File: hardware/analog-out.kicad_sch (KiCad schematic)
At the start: 14 parts, among them U9 TL072

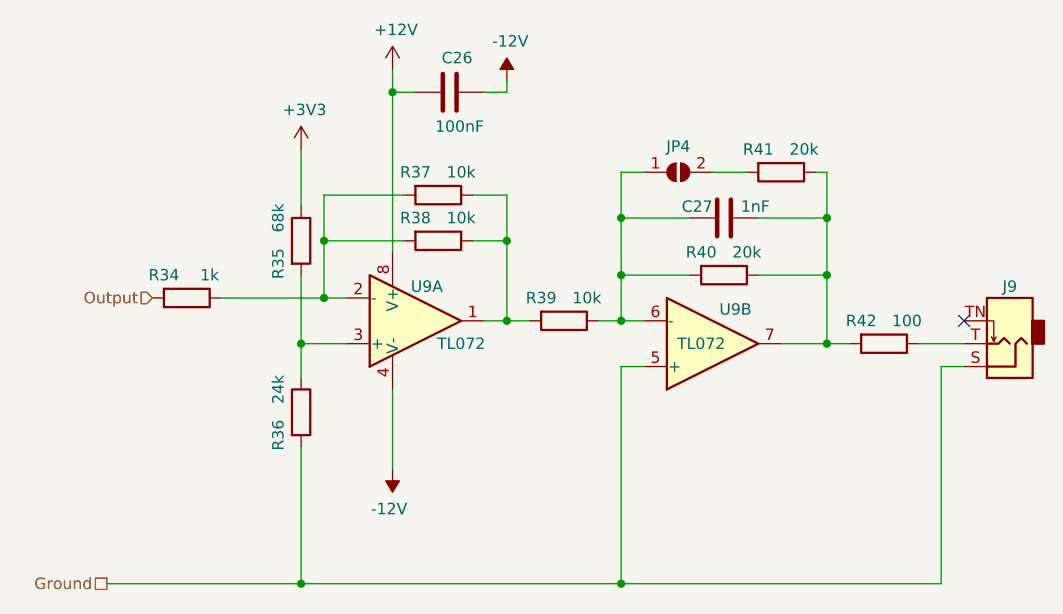
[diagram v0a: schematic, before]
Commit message: First cut of the software. Not changed to RISC-V yet.
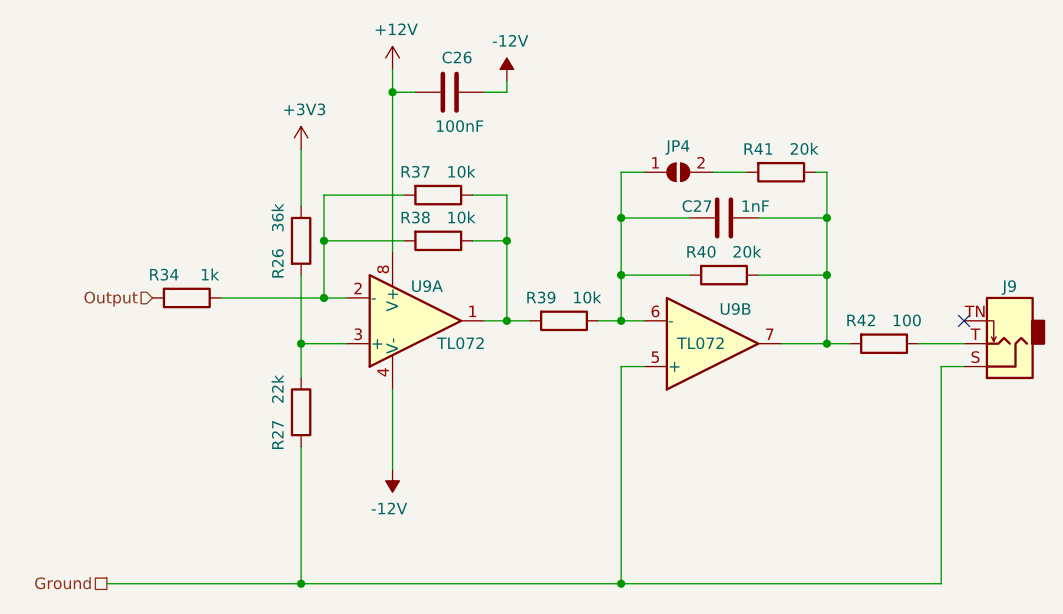
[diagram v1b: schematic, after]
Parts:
- removed R35: 68k, Resistor_SMD:R_0603_1608Metric, symbol Device:R
- removed R36: 24k, Resistor_SMD:R_0603_1608Metric, symbol Device:R
- added R26: 36k, Resistor_SMD:R_0603_1608Metric, symbol Device:R
- added R27: 22k, Resistor_SMD:R_0603_1608Metric, symbol Device:R
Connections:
- net +3V3: now also R26.1
- net Ground: now also R27.2
- net at U9.3 (+): now also R26.2, R27.1
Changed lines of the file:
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@@
     (effects (font (size 1.27 1.27)) (justify right))
+  )
+  (symbol (lib_id "Device:R") (at 55.88 54.61 0) (unit 1)
+    (in_bom yes) (on_board yes)
+    (property "Reference" "R26" (id 0) (at 53.34 57.15 90))
+    (property "Value" "36k" (id 1) (at 53.34 52.07 90))
+    (property "Footprint" "Resistor_SMD:R_0603_1608Metric" (id 2) (at 54.102 54.61 90)
+      (effects (font (size 1.27 1.27)) hide)
+    )
+    (property "Datasheet" "~" (id 3) (at 55.88 54.61 0)
+      (effects (font (size 1.27 1.27)) hide)
+    )
+    (property "LCSC" "C23147" (id 4) (at 55.88 54.61 90)
+      (effects (font (size 1.27 1.27)) hide)
+    )
+    (pin "1")
+    (pin "2")
   )
   (symbol (lib_id "Device:R") (at 120.65 66.04 270) (unit 1)
@@
     )
     (property "LCSC" "C22775" (id 4) (at 120.65 66.04 90)
+      (effects (font (size 1.27 1.27)) hide)
+    )
+    (pin "1")
+    (pin "2")
+  )
+  (symbol (lib_id "Device:R") (at 55.88 73.66 0) (unit 1)
+    (in_bom yes) (on_board yes)
+    (property "Reference" "R27" (id 0) (at 53.34 76.2 90))
+    (property "Value" "22k" (id 1) (at 53.34 71.12 90))
+    (property "Footprint" "Resistor_SMD:R_0603_1608Metric" (id 2) (at 54.102 73.66 90)
+      (effects (font (size 1.27 1.27)) hide)
+    )
+    (property "Datasheet" "~" (id 3) (at 55.88 73.66 0)
+      (effects (font (size 1.27 1.27)) hide)
+    )
+    (property "LCSC" "C31850" (id 4) (at 55.88 73.66 90)
       (effects (font (size 1.27 1.27)) hide)
     )
@@
     (pin "2")
   )
-  (symbol (lib_id "Device:R") (at 55.88 73.66 0) (unit 1)
-    (in_bom yes) (on_board yes)
-    (property "Reference" "R36" (id 0) (at 53.34 76.2 90))
-    (property "Value" "24k" (id 1) (at 53.34 71.12 90))
-    (property "Footprint" "Resistor_SMD:R_0603_1608Metric" (id 2) (at 54.102 73.66 90)
-      (effects (font (size 1.27 1.27)) hide)
-    )
-    (property "Datasheet" "~" (id 3) (at 55.88 73.66 0)
-      (effects (font (size 1.27 1.27)) hide)
-    )
-    (property "LCSC" "C23352" (id 4) (at 55.88 73.66 90)
-      (effects (font (size 1.27 1.27)) hide)
-    )
-    (pin "1")
-    (pin "2")
-  )
   (symbol (lib_id "Amplifier_Operational:TL072") (at 68.58 63.5 0) (mirror x) (unit 1)
     (in_bom yes) (on_board yes)
@@
       (effects (font (size 1.27 1.27)) hide)
     )
-    (pin "1")
-    (pin "2")
-  )
-  (symbol (lib_id "Device:R") (at 55.88 54.61 0) (unit 1)
-    (in_bom yes) (on_board yes)
-    (property "Reference" "R35" (id 0) (at 53.34 57.15 90))
-    (property "Value" "68k" (id 1) (at 53.34 52.07 90))
-    (property "Footprint" "Resistor_SMD:R_0603_1608Metric" (id 2) (at 54.102 54.61 90)
-      (effects (font (size 1.27 1.27)) hide)
-    )
-    (property "Datasheet" "~" (id 3) (at 55.88 54.61 0)
-      (effects (font (size 1.27 1.27)) hide)
-    )
-    (property "LCSC" "C23231" (id 4) (at 55.88 54.61 90)
-      (effects (font (size 1.27 1.27)) hide)
-    )
